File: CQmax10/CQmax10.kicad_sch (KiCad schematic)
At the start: 0 parts

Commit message: schematics
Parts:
- added J1, J2, J3, J4, J5, J6: ~, kicad8-2:Pmod_socket, symbol kicad8-2:Pmod_Socket
- added J7, J8: Conn_02x25_Odd_Even, Connector_PinSocket_2.54mm:PinSocket_2x25_P2.54mm_Vertical, symbol Connector_Generic:Conn_02x25_Odd_Even

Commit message: schematics
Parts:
- added CN2: Conn_02x25_Odd_Even, Connector_PinSocket_2.54mm:PinSocket_2x25_P2.54mm_Vertical, symbol Connector_Generic:Conn_02x25_Odd_Even
- added D1, D2, D3, D4: LED, LED_SMD:LED_0603_1608Metric_Pad1.05x0.95mm_HandSolder, symbol Device:LED
- added J7: Conn_02x25_Odd_Even, Connector_PinHeader_2.54mm:PinHeader_2x25_P2.54mm_Vertical, symbol Connector_Generic:Conn_02x25_Odd_Even
- added R1, R2, R3, R4: R, Resistor_SMD:R_0603_1608Metric_Pad0.98x0.95mm_HandSolder, symbol Device:R
- added R5, R6, R7, R8: 10k, Resistor_SMD:R_0603_1608Metric_Pad0.98x0.95mm_HandSolder, symbol Device:R
- added S1, S2, S3, S4: TVBP06-B043CW-B, TVBP06B043CWB, symbol kicad8:TVBP06-B043CW-B
- J8: footprint Connector_PinSocket_2.54mm:PinSocket_2x25_P2.54mm_Vertical -> Connector_PinHeader_2.54mm:PinHeader_2x25_P2.54mm_Vertical
- renumbered J7 to CN1
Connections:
- net GND: now also CN1.1 (Pin_1), CN1.19 (Pin_19), CN1.2 (Pin_2), CN1.20 (Pin_20), CN1.35 (Pin_35), CN1.36 (Pin_36), CN1.49 (Pin_49), CN1.50 (Pin_50), J8.1 (Pin_1), J8.19 (Pin_19), J8.2 (Pin_2), J8.20 (Pin_20), J8.35 (Pin_35), J8.36 (Pin_36), J8.49 (Pin_49), J8.50 (Pin_50), CN2.1 (Pin_1), CN2.19 (Pin_19), CN2.2 (Pin_2), CN2.20 (Pin_20), CN2.35 (Pin_35), CN2.36 (Pin_36), CN2.49 (Pin_49), CN2.50 (Pin_50), J7.1 (Pin_1), J7.19 (Pin_19), J7.2 (Pin_2), J7.20 (Pin_20), J7.35 (Pin_35), J7.36 (Pin_36), J7.49 (Pin_49), J7.50 (Pin_50), S1.1 (COM), S2.1 (COM), S3.1 (COM), S4.1 (COM)
- net IOPIN7: now reaches J8.10 (Pin_10)
- net IOPIN7: now also CN2.10 (Pin_10)
- net IOPIN140: now reaches J8.11 (Pin_11)
- net IOPIN140: now also CN2.11 (Pin_11)
- net IOPIN141: now reaches J8.12 (Pin_12)
- net IOPIN141: now also CN2.12 (Pin_12)
- net IOPIN134: now reaches J8.13 (Pin_13)
- net IOPIN134: now also CN2.13 (Pin_13)
- net IOPIN135: now reaches J8.14 (Pin_14)
- net IOPIN135: now also CN2.14 (Pin_14)
- net IOPIN131: now reaches J8.15 (Pin_15)
- net IOPIN131: now also CN2.15 (Pin_15)
- net IOPIN132: now reaches J8.16 (Pin_16)
- net IOPIN132: now also CN2.16 (Pin_16)
- net IOPIN127: now reaches J8.17 (Pin_17)
- net IOPIN127: now also CN2.17 (Pin_17)
- net IOPIN130: now reaches J8.18 (Pin_18)
- net IOPIN130: now also CN2.18 (Pin_18)
- net IOPIN124: now reaches J8.21 (Pin_21)
- net IOPIN124: now also CN2.21 (Pin_21)
- net IOPIN126: now reaches J8.22 (Pin_22)
- net IOPIN126: now also CN2.22 (Pin_22)
- net IOPIN122: now reaches J8.23 (Pin_23)
- net IOPIN122: now also CN2.23 (Pin_23)
- net IOPIN123: now reaches J8.24 (Pin_24)
- net IOPIN123: now also CN2.24 (Pin_24)
- net IOPIN120: now reaches J8.25 (Pin_25)
- net IOPIN120: now also CN2.25 (Pin_25)
- net IOPIN121: now reaches J8.26 (Pin_26)
- net IOPIN121: now also CN2.26 (Pin_26)
- net IOPIN118: now reaches J8.27 (Pin_27)
- net IOPIN118: now also CN2.27 (Pin_27)
- net IOPIN119: now reaches J8.28 (Pin_28)
- net IOPIN119: now also CN2.28 (Pin_28)
- net IOPIN113: now reaches J8.29 (Pin_29)
- net IOPIN113: now also CN2.29 (Pin_29)
- net IOPIN13: now reaches J8.3 (Pin_3)
- net IOPIN13: now also CN2.3 (Pin_3)
- net IOPIN114: now reaches J8.30 (Pin_30)
- net IOPIN114: now also CN2.30 (Pin_30)
- net IOPIN111: now reaches J8.31 (Pin_31)
- net IOPIN111: now also CN2.31 (Pin_31)
- net IOPIN112: now reaches J8.32 (Pin_32)
- net IOPIN112: now also CN2.32 (Pin_32)
- net IOPIN106: now reaches J8.33 (Pin_33)
- net IOPIN106: now also CN2.33 (Pin_33)
- net IOPIN110: now reaches J8.34 (Pin_34)
- net IOPIN110: now also CN2.34 (Pin_34)
- net IOPIN102: now reaches J8.37 (Pin_37)
- net IOPIN102: now also CN2.37 (Pin_37)
- net IOPIN105: now reaches J8.38 (Pin_38)
- net IOPIN105: now also CN2.38 (Pin_38)
- net IOPIN100: now reaches J8.39 (Pin_39)
- net IOPIN100: now also CN2.39 (Pin_39)
- net IOPIN14: now reaches J8.4 (Pin_4)
- net IOPIN14: now also CN2.4 (Pin_4)
- net IOPIN101: now reaches J8.40 (Pin_40)
- net IOPIN101: now also CN2.40 (Pin_40)
- net IOPIN98: now reaches J8.41 (Pin_41)
- net IOPIN98: now also CN2.41 (Pin_41)
- net IOPIN99: now reaches J8.42 (Pin_42)
- net IOPIN99: now also CN2.42 (Pin_42)
- net IOPIN96: now reaches J8.43 (Pin_43)
- net IOPIN96: now also CN2.43 (Pin_43)
- net IOPIN97: now reaches J8.44 (Pin_44)
- net IOPIN97: now also CN2.44 (Pin_44)
- net IOPIN92: now reaches J8.45 (Pin_45)
- net IOPIN92: now also CN2.45 (Pin_45)
- net IOPIN93: now reaches J8.46 (Pin_46)
- net IOPIN93: now also CN2.46 (Pin_46)
- net IOPIN90: now reaches J8.47 (Pin_47)
- net IOPIN90: now also CN2.47 (Pin_47)
- net IOPIN91: now reaches J8.48 (Pin_48)
- net IOPIN91: now also CN2.48 (Pin_48)
- net IOPIN11: now reaches J8.5 (Pin_5)
- net IOPIN11: now also CN2.5 (Pin_5)
- net IOPIN12: now reaches J8.6 (Pin_6)
- net IOPIN12: now also CN2.6 (Pin_6)
- net IOPIN8: now reaches J8.7 (Pin_7)
- net IOPIN8: now also CN2.7 (Pin_7)
- net IOPIN10: now reaches J8.8 (Pin_8)
- net IOPIN10: now also CN2.8 (Pin_8)
- net IOPIN6: now reaches J8.9 (Pin_9)
- net IOPIN6: now also CN2.9 (Pin_9)
- net IOPIN30: now reaches CN1.10 (Pin_10)
- net IOPIN30: now also J7.10 (Pin_10), R7.2, S3.2 (NO)
- net IOPIN38: now reaches CN1.11 (Pin_11)
- net IOPIN38: now also D4.1 (K), J7.11 (Pin_11)
- net IOPIN33: now reaches CN1.12 (Pin_12)
- net IOPIN33: now also J7.12 (Pin_12), R8.2, S4.2 (NO)
- net IOPIN41: now reaches CN1.13 (Pin_13)
- net IOPIN41: now also J7.13 (Pin_13)
- net IOPIN39: now reaches CN1.14 (Pin_14)
- net IOPIN39: now also J7.14 (Pin_14)
- net IOPIN44: now reaches CN1.15 (Pin_15)
- net IOPIN44: now also J7.15 (Pin_15)
- net IOPIN43: now reaches CN1.16 (Pin_16)
- net IOPIN43: now also J7.16 (Pin_16)
- net IOPIN46: now reaches CN1.17 (Pin_17)
- net IOPIN46: now also J7.17 (Pin_17)
- net IOPIN45: now reaches CN1.18 (Pin_18)
- net IOPIN45: now also J7.18 (Pin_18)
- net IOPIN48: now reaches CN1.21 (Pin_21)
- net IOPIN48: now also J7.21 (Pin_21)
- net IOPIN47: now reaches CN1.22 (Pin_22)
- net IOPIN47: now also J7.22 (Pin_22)
- net IOPIN52: now reaches CN1.23 (Pin_23)
- net IOPIN52: now also J7.23 (Pin_23)
- net IOPIN50: now reaches CN1.24 (Pin_24)
- net IOPIN50: now also J7.24 (Pin_24)
- net IOPIN55: now reaches CN1.25 (Pin_25)
- net IOPIN55: now also J7.25 (Pin_25)
- net IOPIN54: now reaches CN1.26 (Pin_26)
- net IOPIN54: now also J7.26 (Pin_26)
- net IOPIN57: now reaches CN1.27 (Pin_27)
- net IOPIN57: now also J7.27 (Pin_27)
- net IOPIN56: now reaches CN1.28 (Pin_28)
- net IOPIN56: now also J7.28 (Pin_28)
- net IOPIN59: now reaches CN1.29 (Pin_29)
- net IOPIN59: now also J7.29 (Pin_29)
- net +3V3: now reaches CN1.3 (Pin_3)
- net +3V3: now also CN1.4 (Pin_4), J7.3 (Pin_3), J7.4 (Pin_4), R1.2, R2.2, R3.2, R4.2, R5.1, R6.1, R7.1, R8.1
- net IOPIN58: now reaches CN1.30 (Pin_30)
- net IOPIN58: now also J7.30 (Pin_30)
- net IOPIN61: now reaches CN1.31 (Pin_31)
- net IOPIN61: now also J7.31 (Pin_31)
- net IOPIN60: now reaches CN1.32 (Pin_32)
- net IOPIN60: now also J7.32 (Pin_32)
- net IOPIN64: now reaches CN1.33 (Pin_33)
- net IOPIN64: now also J7.33 (Pin_33)
- net IOPIN62: now reaches CN1.34 (Pin_34)
- net IOPIN62: now also J7.34 (Pin_34)
- net IOPIN66: now reaches CN1.37 (Pin_37)
- net IOPIN66: now also J7.37 (Pin_37)
- net IOPIN65: now reaches CN1.38 (Pin_38)
- net IOPIN65: now also J7.38 (Pin_38)
- net IOPIN70: now reaches CN1.39 (Pin_39)
- net IOPIN70: now also J7.39 (Pin_39)
- net IOPIN69: now reaches CN1.40 (Pin_40)
- net IOPIN69: now also J7.40 (Pin_40)
- net IOPIN75: now reaches CN1.41 (Pin_41)
- net IOPIN75: now also J7.41 (Pin_41)
- net IOPIN74: now reaches CN1.42 (Pin_42)
- net IOPIN74: now also J7.42 (Pin_42)
- net IOPIN77: now reaches CN1.43 (Pin_43)
- net IOPIN77: now also J7.43 (Pin_43)
- net IOPIN76: now reaches CN1.44 (Pin_44)
- net IOPIN76: now also J7.44 (Pin_44)
- net IOPIN79: now reaches CN1.45 (Pin_45)
- net IOPIN79: now also J7.45 (Pin_45)
- net IOPIN78: now reaches CN1.46 (Pin_46)
- net IOPIN78: now also J7.46 (Pin_46)
- net IOPIN81: now reaches CN1.47 (Pin_47)
- net IOPIN81: now also J7.47 (Pin_47)
- net IOPIN80: now reaches CN1.48 (Pin_48)
- net IOPIN80: now also J7.48 (Pin_48)
- net IOPIN27: now reaches CN1.5 (Pin_5)
- net IOPIN27: now also D1.1 (K), J7.5 (Pin_5)
- net IOPIN26: now reaches CN1.6 (Pin_6)
- net IOPIN26: now also J7.6 (Pin_6), R5.2, S1.2 (NO)
- net IOPIN29: now reaches CN1.7 (Pin_7)
- net IOPIN29: now also D2.1 (K), J7.7 (Pin_7)
- net IOPIN28: now reaches CN1.8 (Pin_8)
- net IOPIN28: now also J7.8 (Pin_8), R6.2, S2.2 (NO)
- net IOPIN32: now reaches CN1.9 (Pin_9)
- net IOPIN32: now also D3.1 (K), J7.9 (Pin_9)
- new net: D4.2 (A), R4.1
- new net: D3.2 (A), R3.1
- new net: D1.2 (A), R1.1
- new net: D2.2 (A), R2.1
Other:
- moved on the sheet: CN1

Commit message: schematics
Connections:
- net IOPIN10: now also J3.4 (Pin_4)
- net IOPIN100: now also J4.7 (Pin_7)
- net IOPIN101: now also J4.8 (Pin_8)
- net IOPIN105: now also J4.9 (Pin_9)
- net IOPIN106: now also J4.10 (Pin_10)
- net IOPIN11: now also J3.7 (Pin_7)
- net IOPIN12: now also J3.8 (Pin_8)
- net IOPIN127: now also J6.1 (Pin_1)
- net IOPIN13: now also J3.9 (Pin_9)
- net IOPIN130: now also J6.2 (Pin_2)
- net IOPIN131: now also J6.3 (Pin_3)
- net IOPIN132: now also J6.4 (Pin_4)
- net IOPIN134: now also J6.7 (Pin_7)
- net IOPIN135: now also J6.8 (Pin_8)
- net IOPIN14: now also J3.10 (Pin_10)
- net IOPIN140: now also J6.9 (Pin_9)
- net IOPIN141: now also J6.10 (Pin_10)
- net IOPIN26: no longer R5.2, S1.2 (NO)
- net IOPIN27: no longer D1.1 (K)
- net IOPIN28: no longer R6.2, S2.2 (NO)
- net IOPIN29: no longer D2.1 (K)
- net IOPIN30: now also R5.2, S1.2 (NO); no longer R7.2, S3.2 (NO)
- net IOPIN32: no longer D3.1 (K)
- net IOPIN33: no longer R8.2, S4.2 (NO)
- net IOPIN38: now also J1.1 (Pin_1); no longer D4.1 (K)
- net IOPIN39: now also J1.2 (Pin_2)
- net IOPIN41: now also J1.3 (Pin_3)
- net IOPIN43: now also J1.4 (Pin_4)
- net IOPIN44: now also J1.7 (Pin_7)
- net IOPIN45: now also J1.8 (Pin_8)
- net IOPIN46: now also J1.9 (Pin_9)
- net IOPIN47: now also J1.10 (Pin_10)
- net IOPIN48: now also R6.2, S2.2 (NO)
- net IOPIN50: now also J2.1 (Pin_1)
- net IOPIN52: now also J2.2 (Pin_2)
- net IOPIN54: now also R7.2, S3.2 (NO)
- net IOPIN55: now also J2.3 (Pin_3)
- net IOPIN56: now also J2.4 (Pin_4)
- net IOPIN57: now also J2.7 (Pin_7)
- net IOPIN58: now also J2.8 (Pin_8)
- net IOPIN59: now also J2.9 (Pin_9)
- net IOPIN6: now also J3.1 (Pin_1)
- net IOPIN60: now also J2.10 (Pin_10)
- net IOPIN62: now also R8.2, S4.2 (NO)
- net IOPIN7: now also J3.2 (Pin_2)
- net IOPIN74: now also J5.1 (Pin_1)
- net IOPIN75: now also J5.2 (Pin_2)
- net IOPIN76: now also J5.3 (Pin_3)
- net IOPIN77: now also J5.4 (Pin_4)
- net IOPIN78: now also J5.7 (Pin_7)
- net IOPIN79: now also J5.8 (Pin_8)
- net IOPIN8: now also J3.3 (Pin_3)
- net IOPIN80: now also J5.9 (Pin_9)
- net IOPIN81: now also J5.10 (Pin_10)
- net IOPIN96: now also J4.1 (Pin_1)
- net IOPIN97: now also J4.2 (Pin_2)
- net IOPIN98: now also J4.3 (Pin_3)
- net IOPIN99: now also J4.4 (Pin_4)
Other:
- moved on the sheet: J1, J2, J3, J4, J5, J6

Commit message: artwork
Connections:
- net +3V3: now also J1.12 (Pin_12), J1.6 (Pin_6), J2.12 (Pin_12), J2.6 (Pin_6), J3.12 (Pin_12), J3.6 (Pin_6), J4.12 (Pin_12), J4.6 (Pin_6), J5.12 (Pin_12), J5.6 (Pin_6), J6.12 (Pin_12), J6.6 (Pin_6)
- net GND: now also J1.11 (Pin_11), J1.5 (Pin_5), J2.11 (Pin_11), J2.5 (Pin_5), J3.11 (Pin_11), J3.5 (Pin_5), J4.11 (Pin_11), J4.5 (Pin_5), J5.11 (Pin_11), J5.5 (Pin_5), J6.11 (Pin_11), J6.5 (Pin_5)
- net IOPIN10: now also J3.9 (Pin_9); no longer J3.4 (Pin_4)
- net IOPIN100: now also J4.8 (Pin_8); no longer J4.7 (Pin_7)
- net IOPIN101: now also J4.7 (Pin_7); no longer J4.8 (Pin_8)
- net IOPIN11: now also J3.2 (Pin_2); no longer J3.7 (Pin_7)
- net IOPIN120: now also D3.1 (K)
- net IOPIN121: now also D4.1 (K)
- net IOPIN122: now also D2.1 (K)
- net IOPIN123: now also D1.1 (K)
- net IOPIN127: now also J6.10 (Pin_10); no longer J6.1 (Pin_1)
- net IOPIN13: now also J3.1 (Pin_1); no longer J3.9 (Pin_9)
- net IOPIN130: now also J6.4 (Pin_4); no longer J6.2 (Pin_2)
- net IOPIN131: now also J6.9 (Pin_9); no longer J6.3 (Pin_3)
- net IOPIN132: now also J6.3 (Pin_3); no longer J6.4 (Pin_4)
- net IOPIN134: now also J6.1 (Pin_1); no longer J6.7 (Pin_7)
- net IOPIN135: now also J6.2 (Pin_2); no longer J6.8 (Pin_8)
- net IOPIN14: now also J3.7 (Pin_7); no longer J3.10 (Pin_10)
- net IOPIN140: now also J6.8 (Pin_8); no longer J6.9 (Pin_9)
- net IOPIN141: now also J6.7 (Pin_7); no longer J6.10 (Pin_10)
- net IOPIN30: now also R8.2, S4.2 (NO); no longer R5.2, S1.2 (NO)
- net IOPIN38: now also J1.4 (Pin_4); no longer J1.1 (Pin_1)
- net IOPIN39: now also J1.9 (Pin_9); no longer J1.2 (Pin_2)
- net IOPIN43: now also J1.8 (Pin_8); no longer J1.4 (Pin_4)
- net IOPIN44: now also J1.2 (Pin_2); no longer J1.7 (Pin_7)
- net IOPIN45: now also J1.7 (Pin_7); no longer J1.8 (Pin_8)
- net IOPIN46: now also J1.1 (Pin_1); no longer J1.9 (Pin_9)
- net IOPIN48: now also R7.2, S3.2 (NO); no longer R6.2, S2.2 (NO)
- net IOPIN50: now also J2.10 (Pin_10); no longer J2.1 (Pin_1)
- net IOPIN52: now also J2.4 (Pin_4); no longer J2.2 (Pin_2)
- net IOPIN54: now also R6.2, S2.2 (NO); no longer R7.2, S3.2 (NO)
- net IOPIN56: now also J2.9 (Pin_9); no longer J2.4 (Pin_4)
- net IOPIN57: now also J2.2 (Pin_2); no longer J2.7 (Pin_7)
- net IOPIN59: now also J2.1 (Pin_1); no longer J2.9 (Pin_9)
- net IOPIN6: now also J3.4 (Pin_4); no longer J3.1 (Pin_1)
- net IOPIN60: now also J2.7 (Pin_7); no longer J2.10 (Pin_10)
- net IOPIN62: now also R5.2, S1.2 (NO); no longer R8.2, S4.2 (NO)
- net IOPIN7: now also J3.10 (Pin_10); no longer J3.2 (Pin_2)
- net IOPIN74: now also J5.9 (Pin_9); no longer J5.1 (Pin_1)
- net IOPIN75: now also J5.10 (Pin_10); no longer J5.2 (Pin_2)
- net IOPIN76: now also J5.4 (Pin_4); no longer J5.3 (Pin_3)
- net IOPIN77: now also J5.3 (Pin_3); no longer J5.4 (Pin_4)
- net IOPIN78: now also J5.8 (Pin_8); no longer J5.7 (Pin_7)
- net IOPIN79: now also J5.2 (Pin_2); no longer J5.8 (Pin_8)
- net IOPIN80: now also J5.1 (Pin_1); no longer J5.9 (Pin_9)
- net IOPIN81: now also J5.7 (Pin_7); no longer J5.10 (Pin_10)
- net IOPIN96: now also J4.3 (Pin_3); no longer J4.1 (Pin_1)
- net IOPIN97: now also J4.4 (Pin_4); no longer J4.2 (Pin_2)
- net IOPIN98: now also J4.1 (Pin_1); no longer J4.3 (Pin_3)
- net IOPIN99: now also J4.2 (Pin_2); no longer J4.4 (Pin_4)
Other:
- moved on the sheet: J3, J4, J6

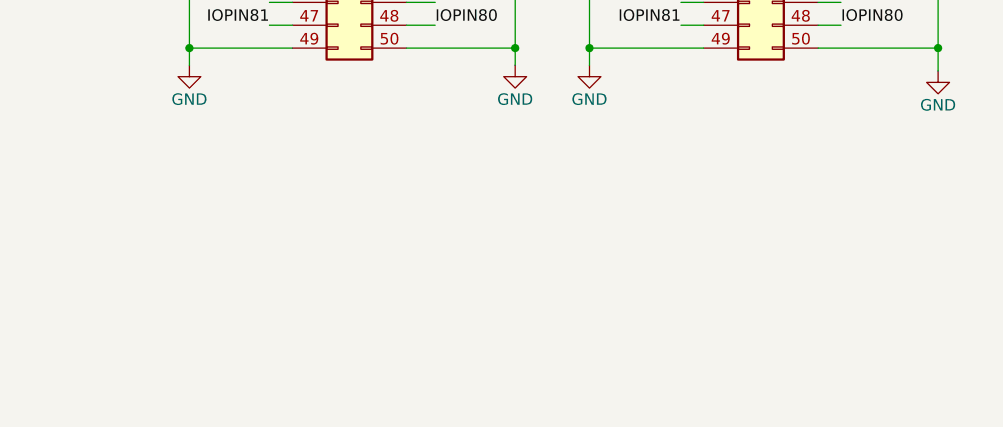
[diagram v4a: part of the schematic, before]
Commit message: add usb-c, 3v3regulater
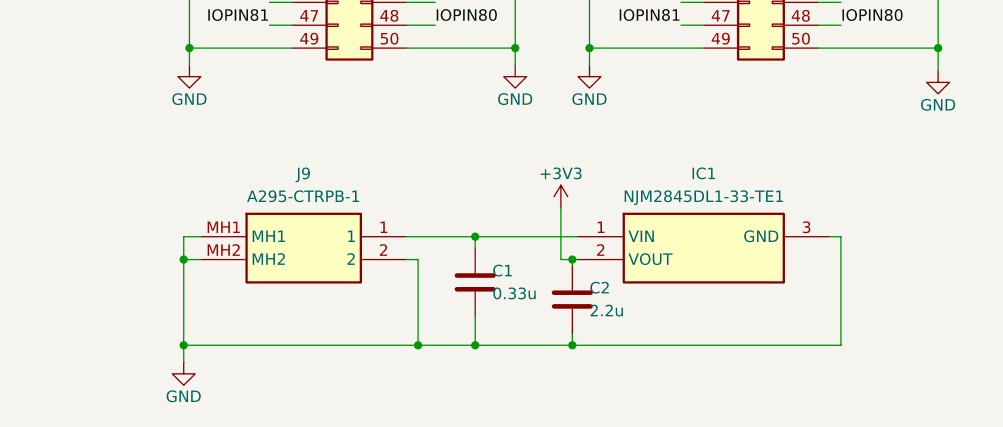
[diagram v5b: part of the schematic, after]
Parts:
- added C1: 0.33u, Capacitor_SMD:C_0603_1608Metric_Pad1.08x0.95mm_HandSolder, symbol Device:C
- added C2: 2.2u, Capacitor_SMD:C_0603_1608Metric_Pad1.08x0.95mm_HandSolder, symbol Device:C
- added IC1: NJM2845DL1-33-TE1, TO-252-3-L1, symbol samacsys:NJM2845DL1-33-TE1
- added J9: A295-CTRPB-1, A295CTRPB1, symbol samacsys:A295-CTRPB-1
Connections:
- net +3V3: now also C2.1, IC1.2 (VOUT)
- net GND: now also C1.2, C2.2, IC1.3 (GND), J9.2, J9.MH1, J9.MH2
- new net: C1.1, IC1.1 (VIN), J9.1

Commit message: add 5v pad
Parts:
- added J10: Conn_01x01_Pin, Connector_PinHeader_2.54mm:PinHeader_1x01_P2.54mm_Vertical, symbol Connector:Conn_01x01_Pin
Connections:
- net at C1.1, IC1.1 (VIN), J9.1: now also J10.1 (Pin_1)
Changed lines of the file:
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@@
 	)
 	(junction
+		(at 116.205 175.26)
+		(diameter 0)
+		(color 0 0 0 0)
+	)
+	(junction
 		(at 182.88 116.205)
 		(diameter 0)
@@
 	(wire
 		(pts
-			(xy 112.395 175.26) (xy 120.015 175.26)
+			(xy 112.395 175.26) (xy 116.205 175.26)
 		)
 		(stroke
@@
 	(wire
 		(pts
+			(xy 116.205 165.1) (xy 116.205 175.26)
+		)
+		(stroke
+			(width 0)
+			(type default)
+		)
+	)
+	(wire
+		(pts
 			(xy 97.155 106.045) (xy 99.695 106.045)
 		)
@@
 	(wire
 		(pts
+			(xy 116.205 175.26) (xy 120.015 175.26)
+		)
+		(stroke
+			(width 0)
+			(type default)
+		)
+	)
+	(wire
+		(pts
 			(xy 240.03 136.525) (xy 240.03 154.305)
 		)
@@
 	(wire
 		(pts
+			(xy 113.665 165.1) (xy 116.205 165.1)
+		)
+		(stroke
+			(width 0)
+			(type default)
+		)
+	)
+	(wire
+		(pts
 			(xy 194.31 118.745) (xy 196.85 118.745)
 		)
@@
 					(unit 1)
 				)
+			)
+		)
+	)
+	(symbol
+		(lib_id "Connector:Conn_01x01_Pin")
+		(at 108.585 165.1 0)
+		(unit 1)
+		(exclude_from_sim no)
+		(in_bom yes)
+		(on_board yes)
+		(dnp no)
+		(fields_autoplaced yes)
+		(property "Reference" "J10"
+			(at 109.22 160.02 0)
+			(effects
+				(font
+					(size 1.27 1.27)
+				)
+			)
+		)
+		(property "Value" "Conn_01x01_Pin"
+			(at 109.22 162.56 0)
+			(effects
+				(font
+					(size 1.27 1.27)
+				)
+			)
+		)
+		(property "Footprint" "Connector_PinHeader_2.54mm:PinHeader_1x01_P2.54mm_Vertical"
+			(at 108.585 165.1 0)
+			(effects
+				(font
+					(size 1.27 1.27)
+				)
+				(hide yes)
+			)
+		)
+		(property "Datasheet" "~"
+			(at 108.585 165.1 0)
+			(effects
+				(font
+					(size 1.27 1.27)
+				)
+				(hide yes)
+			)
+		)
+		(property "Description" "Generic connector, single row, 01x01, script generated"
+			(at 108.585 165.1 0)
+			(effects
+				(font
+					(size 1.27 1.27)
+				)
+				(hide yes)
+			)
+		)
+		(pin "1"
+		)
+		(instances
+			(project ""
+				(path "/b73835bc-423c-4a87-9172-5af94b735525"
+					(reference "J10")
+					(unit 1)
+				)

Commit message: led register value update
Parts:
- R1, R2, R3, R4: value R -> 43
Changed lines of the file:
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@@
 			)
 		)
-		(property "Value" "R"
+		(property "Value" "43"
 			(at 49.53 184.785 90)
 			(effects
@@
 			)
 		)
-		(property "Value" "R"
+		(property "Value" "43"
 			(at 49.53 157.48 90)
 			(effects
@@
 			)
 		)
-		(property "Value" "R"
+		(property "Value" "43"
 			(at 49.53 167.005 90)
 			(effects
@@
 			)
 		)
-		(property "Value" "R"
+		(property "Value" "43"
 			(at 49.53 175.895 90)
 			(effects
